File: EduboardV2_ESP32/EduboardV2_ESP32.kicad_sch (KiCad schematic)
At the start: 14 parts, among them J1 EduboardV2 PCIE UP Board Conn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, SW1 K2-1102SP-C4SC-04, SW2 K2-1102SP-C4SC-04, U1 ESP32-WROOM-E

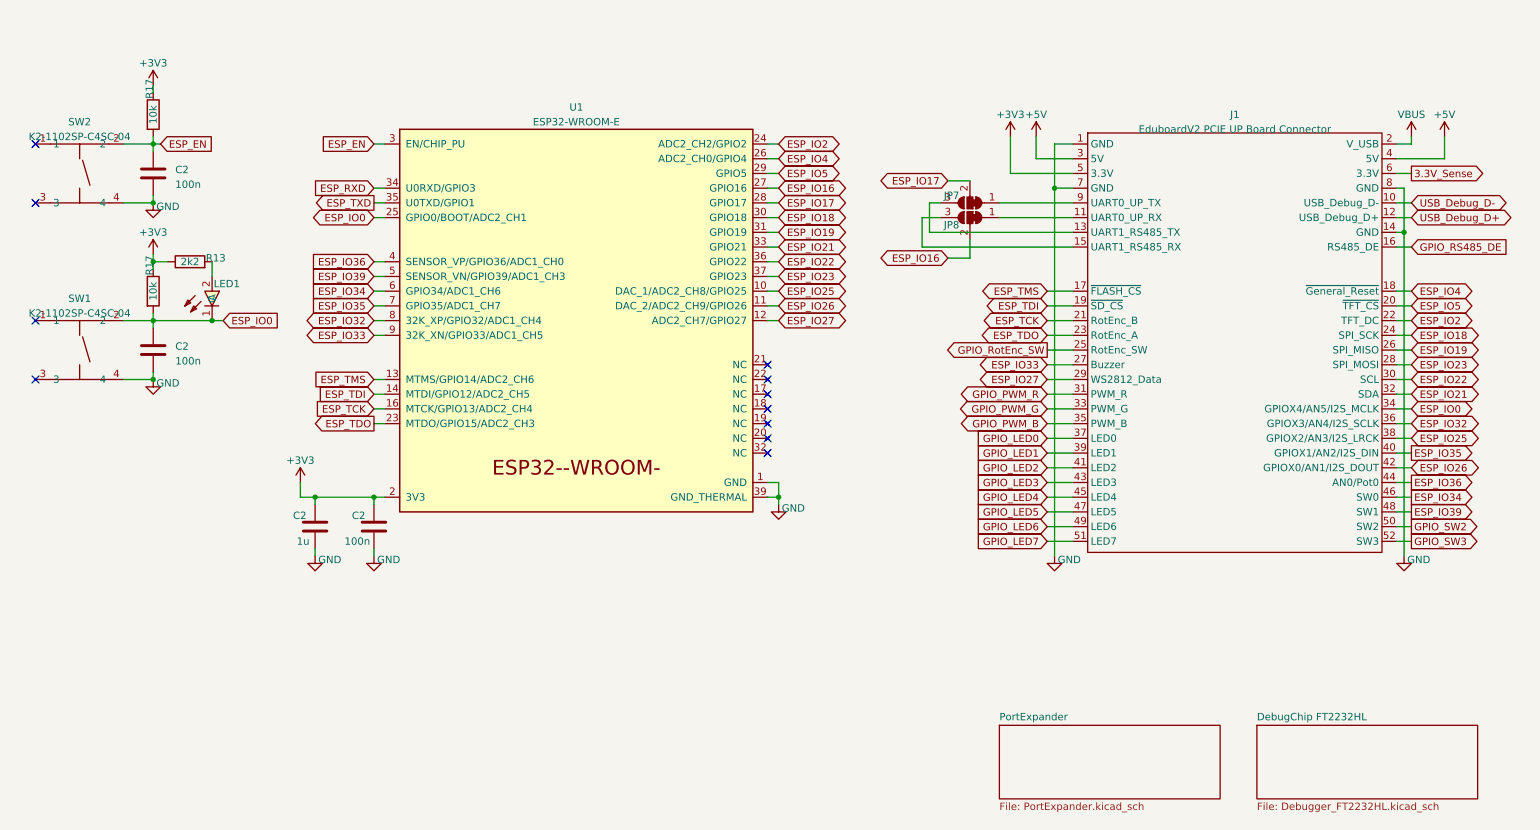
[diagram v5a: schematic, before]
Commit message: rework pin assignement with esp32 pin restrictions in mind. start layout
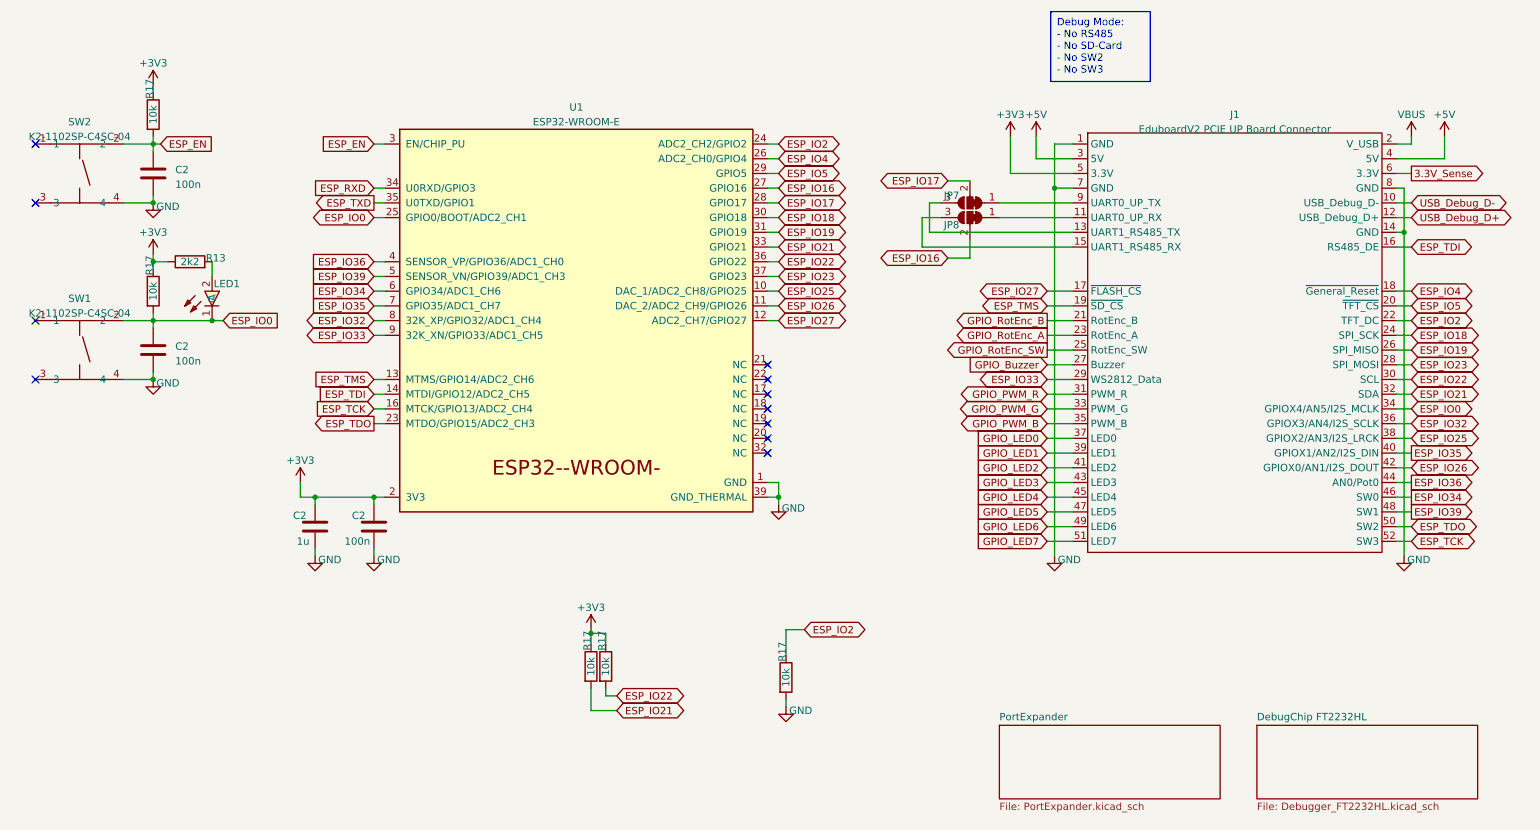
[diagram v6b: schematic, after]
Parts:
- added R17 (x3): 10k, Resistor_SMD:R_0603_1608Metric, symbol Device:R
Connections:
- net GPIO_RS485_DE is gone; now on net ESP_TDI: J1.16 (RS485_DE)
- net GPIO_SW2 is gone; now on net ESP_TDO: J1.50 (SW2)
- net GPIO_SW3 is gone; now on net ESP_TCK: J1.52 (SW3)
- net +3V3: now also R17.1, R17.1
- net ESP_IO2: now also R17.1
- net ESP_IO21: now also R17.2
- net ESP_IO22: now also R17.2
- net ESP_IO27: now also J1.17 (~{FLASH_CS}); no longer J1.29 (WS2812_Data)
- net ESP_IO33: now also J1.29 (WS2812_Data); no longer J1.27 (Buzzer)
- net ESP_TCK: no longer J1.21 (RotEnc_B)
- net ESP_TDI: no longer J1.19 (~{SD_CS})
- net ESP_TDO: no longer J1.23 (RotEnc_A)
- net ESP_TMS: now also J1.19 (~{SD_CS}); no longer J1.17 (~{FLASH_CS})
- net GND: now also R17.2
- new net GPIO_Buzzer: J1.27 (Buzzer)
- new net GPIO_RotEnc_A: J1.23 (RotEnc_A)
- new net GPIO_RotEnc_B: J1.21 (RotEnc_B)

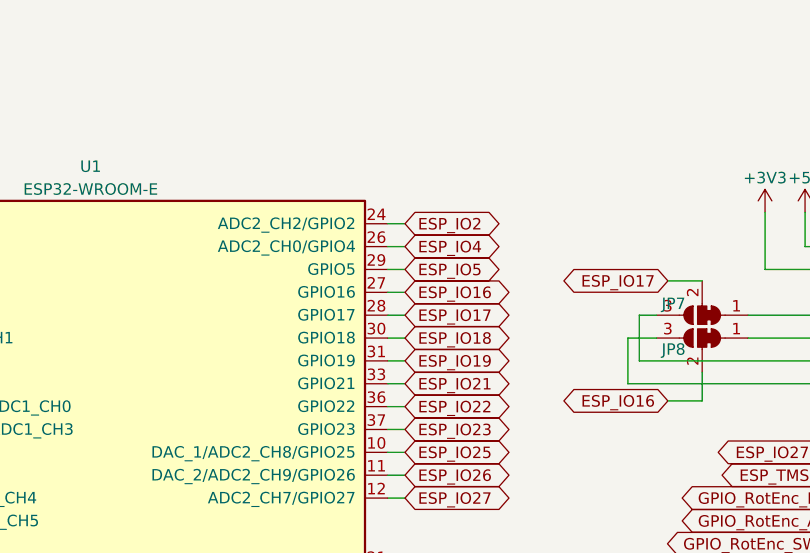
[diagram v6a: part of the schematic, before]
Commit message: resize mPCIE Board Footprint, work on ESP32 UP Board
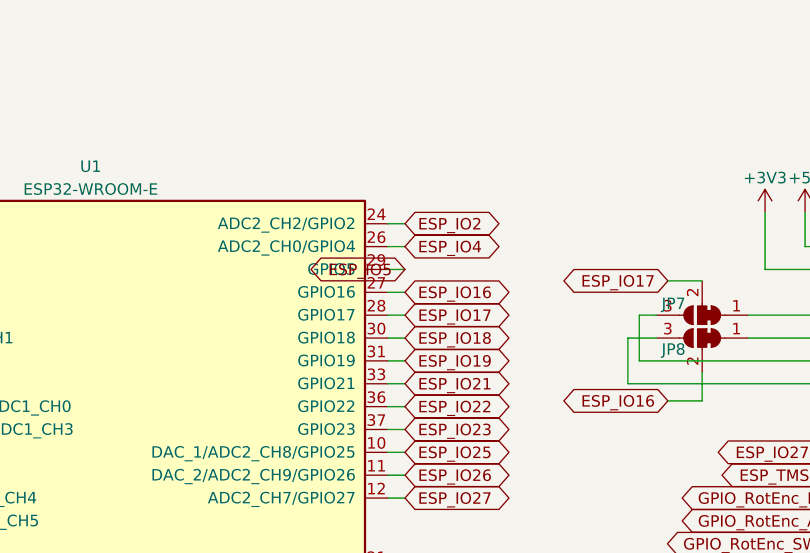
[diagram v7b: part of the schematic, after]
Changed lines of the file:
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@@
     )
   )
-  (global_label "ESP_IO5" (shape bidirectional) (at 146.05 44.45 0) (fields_autoplaced)
-    (effects (font (size 1.27 1.27)) (justify left))
-    (property "Intersheetrefs" "${INTERSHEET_REFS}" (at 157.808 44.45 0)
-      (effects (font (size 1.27 1.27)) (justify left) hide)
+  (global_label "ESP_IO5" (shape bidirectional) (at 146.05 44.45 180) (fields_autoplaced)
+    (effects (font (size 1.27 1.27)) (justify right))
+    (property "Intersheetrefs" "${INTERSHEET_REFS}" (at 134.292 44.45 0)
+      (effects (font (size 1.27 1.27)) (justify right) hide)
     )
   )

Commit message: finalize Layout, fill in most of the critical part info. Replace certain parts with Eduboard kicadlib Parts.
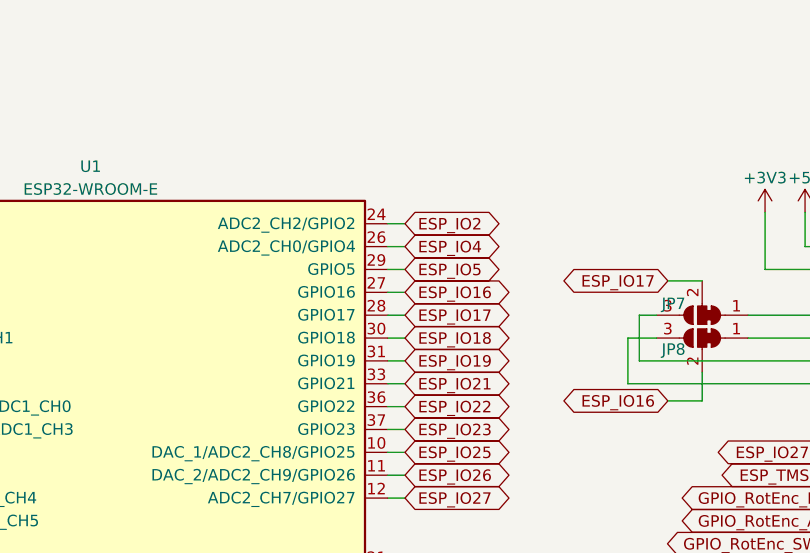
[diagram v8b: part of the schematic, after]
